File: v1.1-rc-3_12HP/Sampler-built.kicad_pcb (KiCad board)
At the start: 4 copper layers, 60.5 x 109.2 mm, 241 parts, among them J10 Eurorack_Power_10pin_Unshroud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, J11 3.5mm_Mono_Switched, J12 3.5mm_Mono_Switched, J13 3.5mm_Mono_Switched, J14 3.5mm_Mono_Switched, J15 3.5mm_Mono_Switched, J16 3.5mm_Mono_Switched, J17 3.5mm_Mono_Switched, J2 3.5mm_Mono_Switched, J3 Conn_01x04, J4 Conn_02x04, J6 3.5mm_Mono_Switched, J7 3.5mm_Mono_Switched, J8 3.5mm_Mono_Switched, J9 3.5mm_Mono_Switched, Q11 Si2347, Q12 Si2318, U1 TL072H, U10 TL072H, U11 TL072H, U12 TL072H, U13 AP62200WU-7, U14 TL072H, U15 TL072H, U16 TL072H, U2 STM32F746IE, U3 TL072H, U4 SDRAM_IS42S16400J-6BLI-TR, U5 TL072H, U6 NCP51460SN33, U8 TL072H, U9 PCM3060PW, Y1 16MHz_18pF_FA238

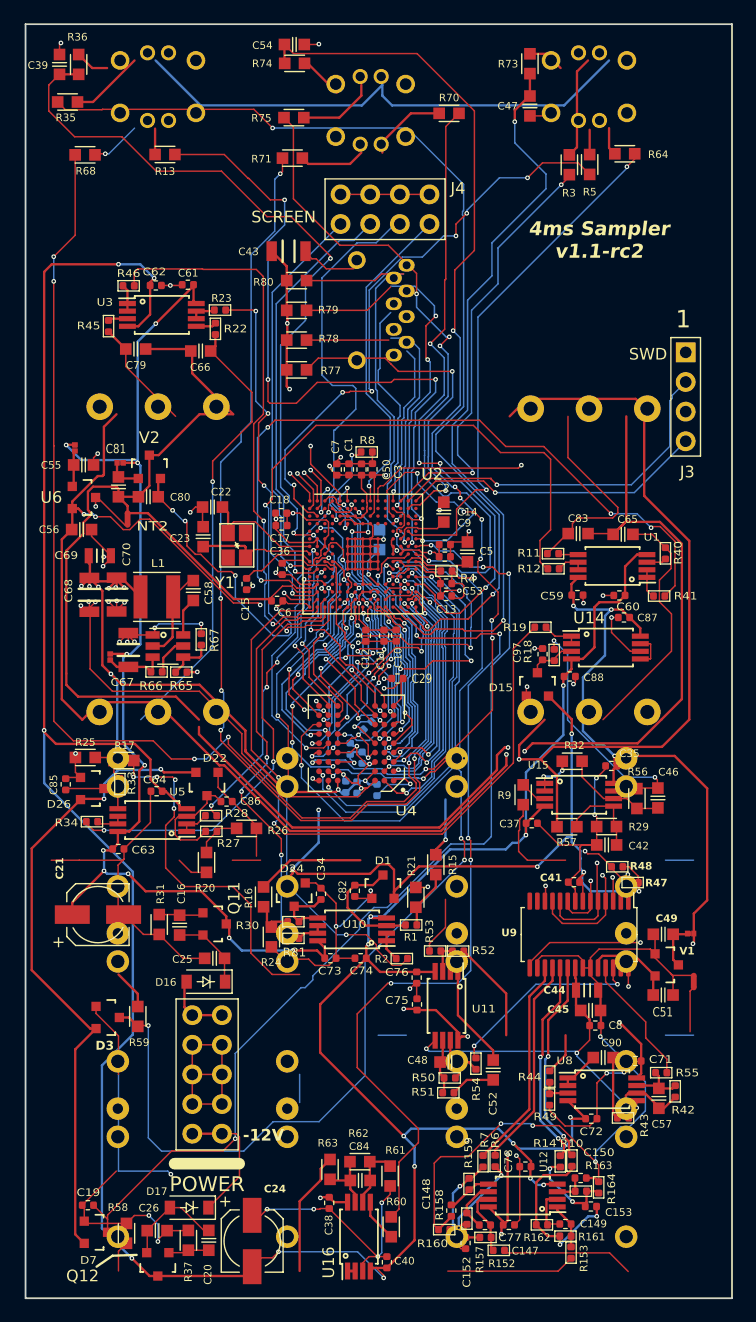
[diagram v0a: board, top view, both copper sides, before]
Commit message: moved components to rough placement, have not started routing
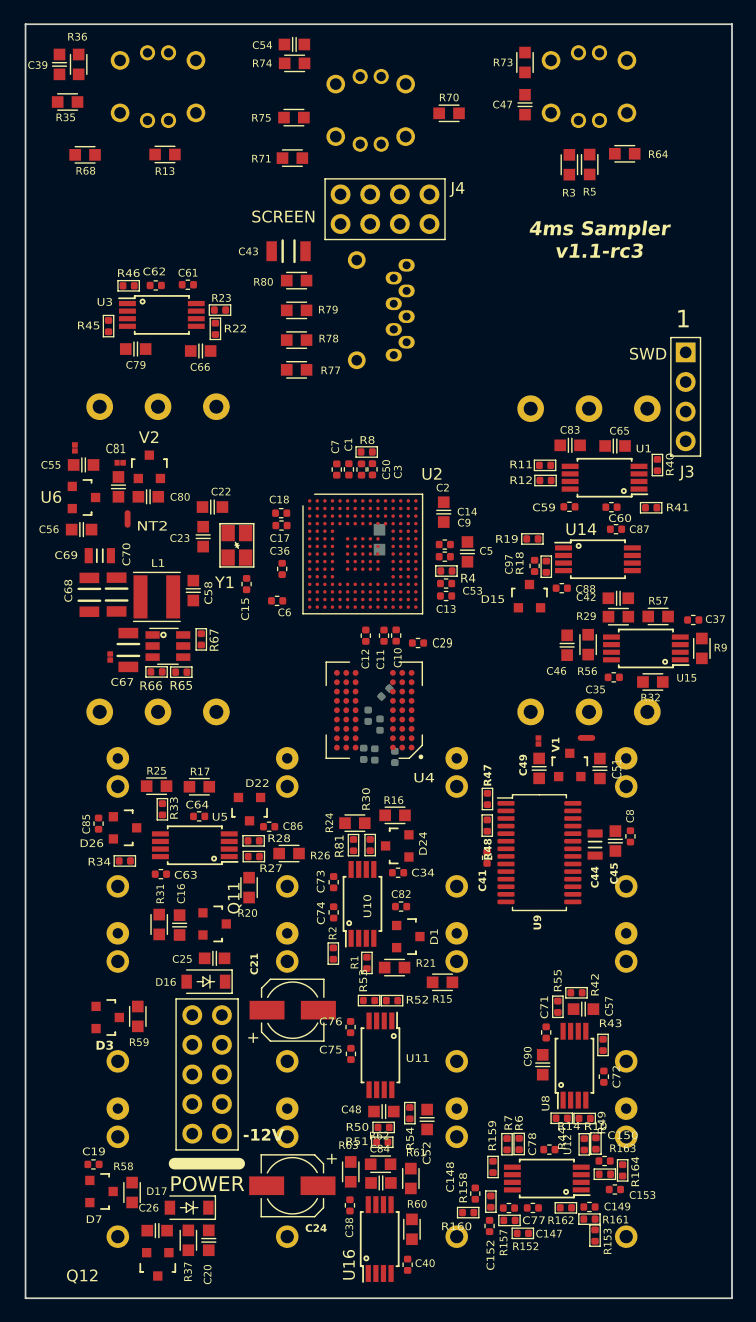
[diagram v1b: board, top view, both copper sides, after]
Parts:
- moved NT1 22.8 mm to (48.1, 61.2), turned to 0 degrees
- moved C37 22.2 mm to (57.2, 51.1), turned to 180 degrees
- moved C42 21.2 mm to (50.8, 49.2), turned to 180 degrees
- moved JP4 21.0 mm to (44.0, 61.4), turned to -90 degrees
- moved C51 20.2 mm to (49.2, 63.8), turned to 90 degrees
- moved R9 19.8 mm to (58.0, 53.5), turned to -90 degrees
- moved R57 19.6 mm to (54.2, 50.8), turned to 0 degrees
- moved V1 19.0 mm to (46.6, 63.5), turned to 0 degrees
- moved C21 18.6 mm to (22.9, 84.5)
- moved R29 18.0 mm to (50.8, 50.8), turned to 180 degrees
- moved C49 17.8 mm to (44.0, 63.8), turned to -90 degrees
- moved C8 16.5 mm to (51.8, 69.6), turned to 90 degrees
- moved C46 15.2 mm to (46.4, 53.2), turned to 90 degrees
- moved C45 14.7 mm to (50.6, 70.0), turned to 90 degrees
- moved R47 14.4 mm to (39.6, 66.4), turned to 90 degrees
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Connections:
- C19 pad 1: GND -> /D2
- D7 pad 3: GND -> /D2
- R58 pad 2: GND -> /D2
- U2 pad G15: GND -> /D2
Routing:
- net GND: track 469.4 -> 0.00 mm, vias 65 -> 0
- net +3V3: track 401.9 -> 0.00 mm, vias 32 -> 0
- net -12VA: track 268.8 -> 0.00 mm, vias 16 -> 0
- net +12V: track 234.3 -> 0.00 mm, vias 20 -> 0
- net VREF+: track 167.8 -> 0.00 mm, vias 6 -> 0
- net GNDADC: track 163.8 -> 0.00 mm, vias 2 -> 0
- net /D7: track 104.9 -> 0.00 mm, vias 6 -> 0
- net /D8: track 90.1 -> 0.00 mm, vias 6 -> 0
- net /D10: track 86.5 -> 0.00 mm, vias 2 -> 0
- net /D13: track 86.2 -> 0.00 mm, vias 4 -> 0
- net /SAI_FS: track 79.1 -> 0.00 mm, vias 2 -> 0
- net /D15: track 77.2 -> 0.00 mm, vias 6 -> 0
- net /SAI_SCK: track 75.9 -> 0.00 mm, vias 2 -> 0
- net /CODEC_RESET: track 73.8 -> 0.00 mm, vias 2 -> 0
- net /SAI_MCLK: track 73.1 -> 0.00 mm, vias 2 -> 0
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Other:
- board text added: "4ms Sampler v1.1-rc3"
- board text removed: "4ms Sampler v1.1-rc2"

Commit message: board routed, running a double check on DRC
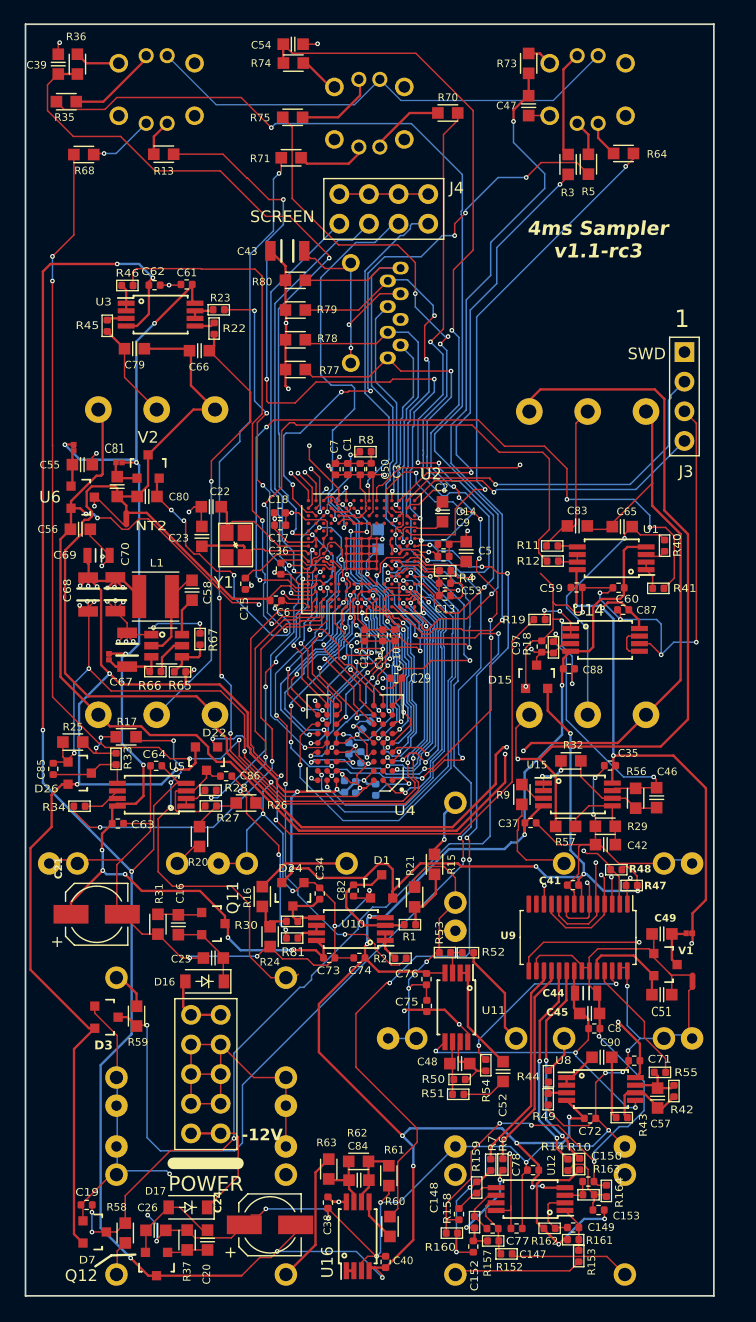
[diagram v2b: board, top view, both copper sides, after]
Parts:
- moved NT1 22.8 mm to (57.2, 82.0), turned to -90 degrees
- moved C37 22.3 mm to (43.3, 68.5), turned to 0 degrees
- moved C42 21.1 mm to (49.7, 70.3), turned to 0 degrees
- moved JP4 20.9 mm to (56.9, 77.9), turned to 180 degrees
- moved C51 20.1 mm to (54.5, 83.2), turned to 0 degrees
- moved R9 19.9 mm to (42.5, 66.0), turned to 90 degrees
- moved R57 19.7 mm to (46.3, 68.8), turned to 180 degrees
- moved V1 19.0 mm to (54.9, 80.6), turned to -90 degrees
- moved C21 18.7 mm to (6.10, 76.3)
- moved R29 18.0 mm to (49.7, 68.7), turned to 0 degrees
- moved C49 17.7 mm to (54.6, 78.0), turned to 180 degrees
- moved C8 16.8 mm to (48.8, 86.1), turned to 0 degrees
- moved C46 15.2 mm to (54.1, 66.3), turned to -90 degrees
- moved C45 14.9 mm to (48.4, 84.8), turned to 0 degrees
- moved R47 14.4 mm to (52.0, 73.8), turned to 0 degrees
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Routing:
- net GND: track 0.00 -> 569.0 mm, vias 0 -> 74
- net +3V3: track 0.00 -> 407.4 mm, vias 0 -> 32
- net -12VA: track 0.00 -> 272.6 mm, vias 0 -> 17
- net +12V: track 0.00 -> 241.6 mm, vias 0 -> 19
- net VREF+: track 0.00 -> 167.4 mm, vias 0 -> 6
- net GNDADC: track 0.00 -> 163.2 mm, vias 0 -> 2
- net /D7: track 0.00 -> 102.7 mm, vias 0 -> 6
- net /D8: track 0.00 -> 88.8 mm, vias 0 -> 6
- net /D2: track 0.00 -> 88.7 mm, vias 0 -> 6
- net /D10: track 0.00 -> 88.1 mm, vias 0 -> 2
- net /D13: track 0.00 -> 84.3 mm, vias 0 -> 4
- net /SAI_FS: track 0.00 -> 79.3 mm, vias 0 -> 2
- net /D15: track 0.00 -> 76.3 mm, vias 0 -> 6
- net /SAI_SCK: track 0.00 -> 76.1 mm, vias 0 -> 2
- net /CODEC_RESET: track 0.00 -> 74.9 mm, vias 0 -> 2
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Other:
- board size 60.5 x 109.2 mm -> 59 x 109 mm

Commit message: verified DRC, fixing silkscreen next
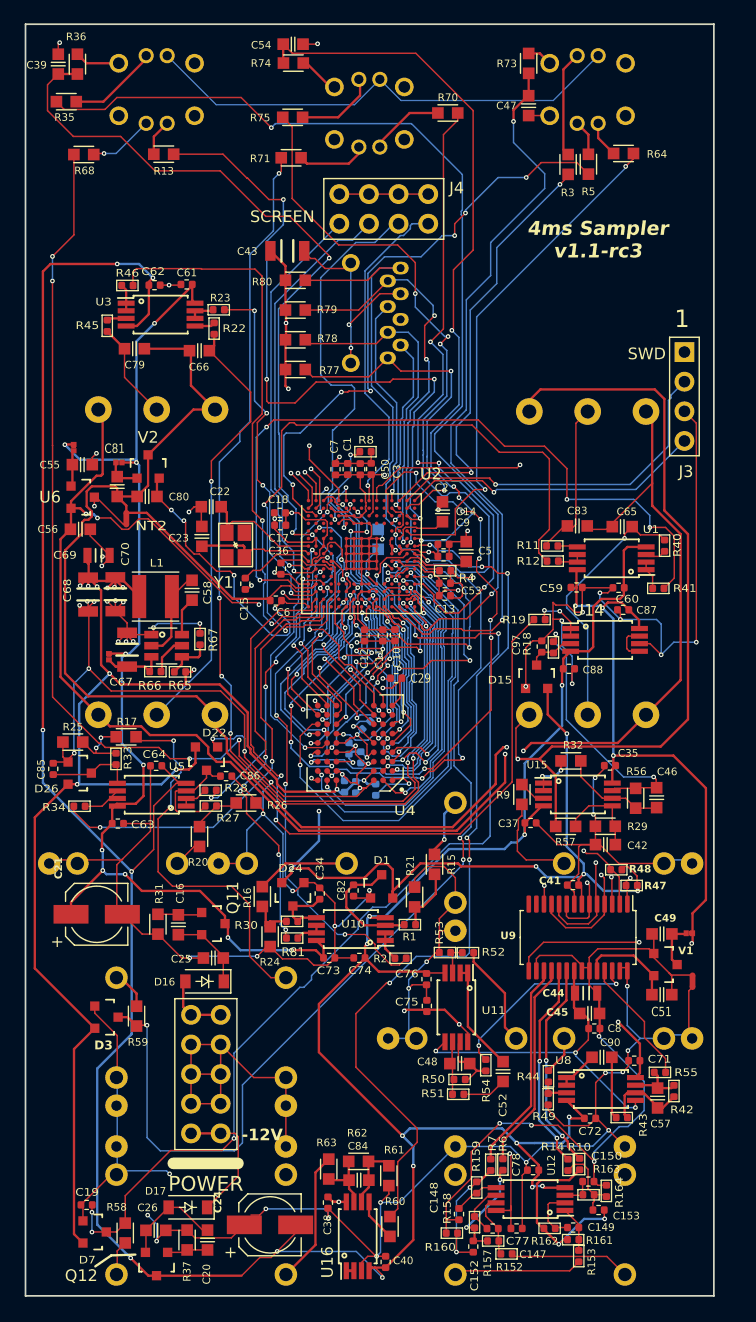
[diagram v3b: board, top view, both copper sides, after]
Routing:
- net GND: track 569.0 -> 562.9 mm
- net GNDADC: track 163.2 -> 161.1 mm
- net -12VA: track 272.6 -> 271.0 mm
- net VREF+: track 167.4 -> 166.0 mm
- net +3V3: track 407.4 -> 406.0 mm, vias 32 -> 31
- net /D17: track 37.0 -> 35.6 mm
- net /D4: track 27.1 -> 25.9 mm
- net Net-(D15-AK): track 5.13 -> 4.03 mm, vias 1 -> 0
- net Net-(U11B--): track 4.79 -> 3.80 mm
- net Net-(C147-Pad1): track 5.65 -> 4.71 mm
- net Net-(PLAY_BUT1-B): track 6.80 -> 5.89 mm
- net Net-(J9-SIG): track 34.2 -> 33.3 mm, vias 3 -> 2
- net +12V: track 241.6 -> 240.9 mm
- net Net-(U12B--): track 4.45 -> 3.79 mm
- net Net-(D22-AK): track 9.56 -> 8.94 mm
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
